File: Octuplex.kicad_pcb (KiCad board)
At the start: 2 copper layers, 140 x 140 mm, 34 parts, among them J1 DIN-5_180degree, J2 DIN-5_180degree, U1 MC68B09, U10 R6522, U11 74LS138, U12 HCPL-2631, U13 74LS251, U14 PCF8584, U15 74LS138, U2 MC68B40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

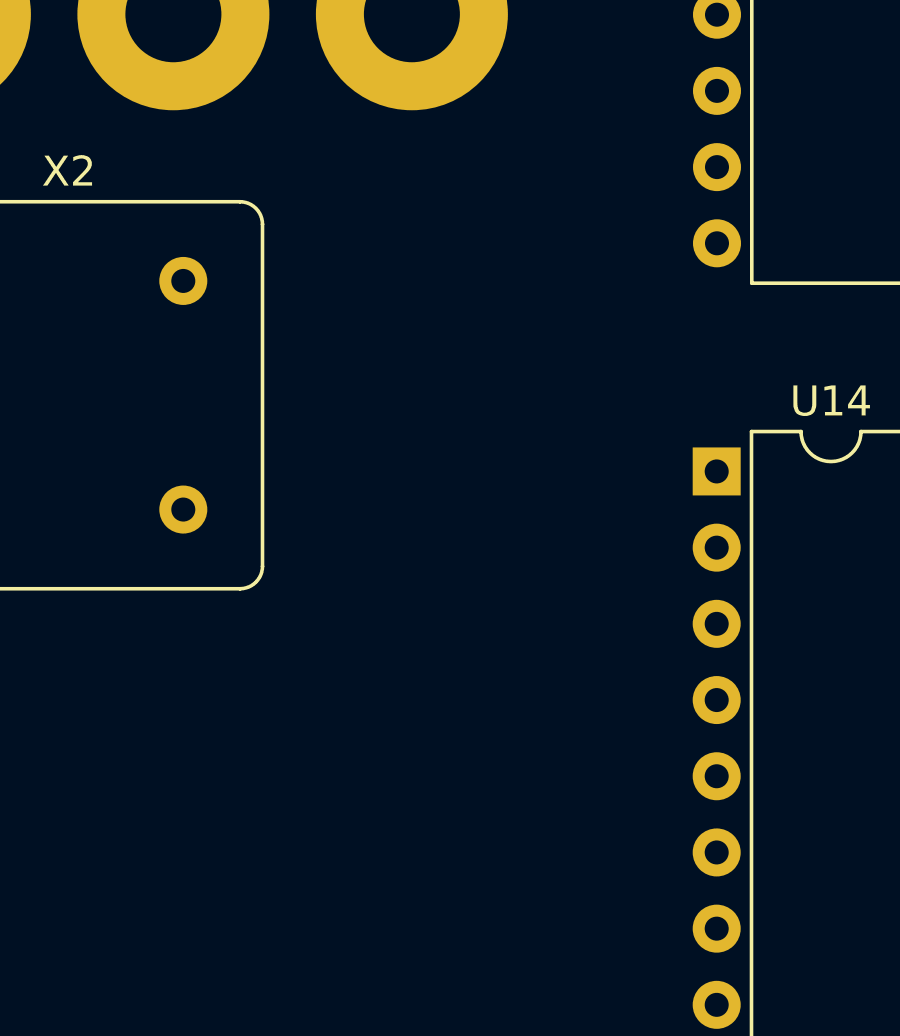
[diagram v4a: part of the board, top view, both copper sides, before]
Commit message: Add ZN428 8-bit DAC.
Add symbol for ZN428 and place it on the GPIO page.
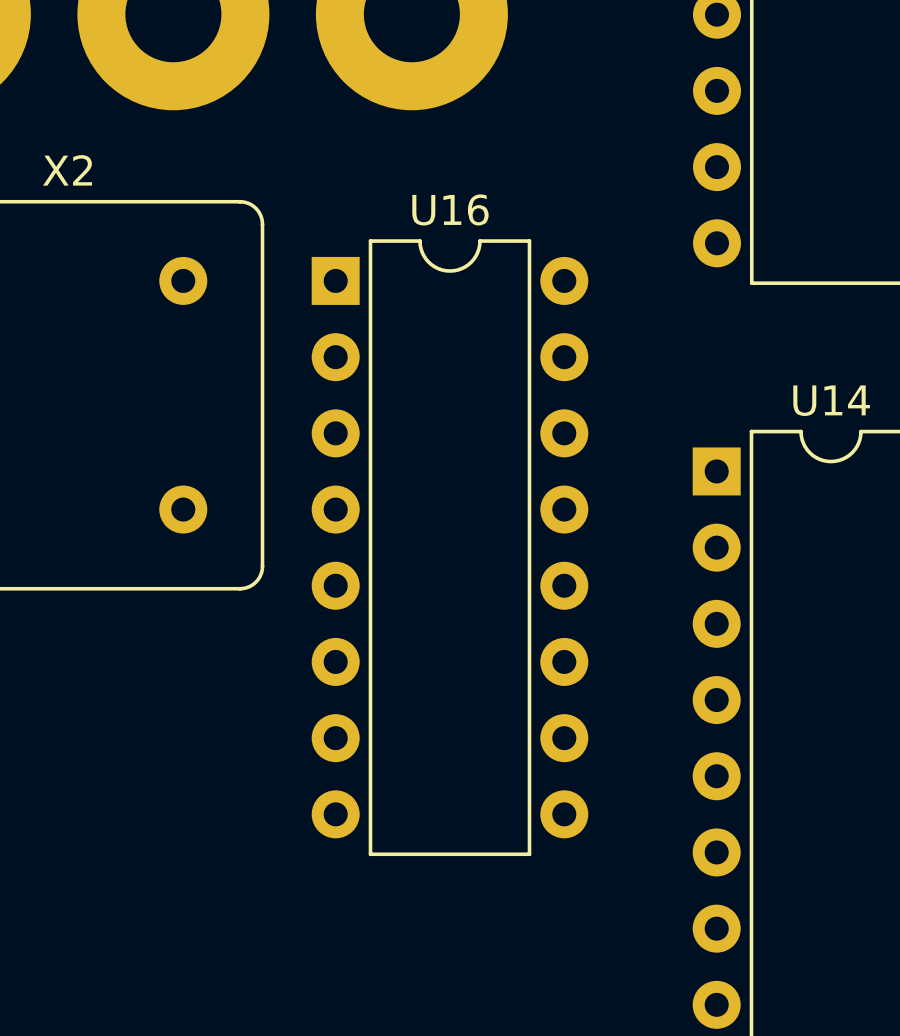
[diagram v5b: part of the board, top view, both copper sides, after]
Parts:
- added U16: ZN428, Package_DIP:DIP-16_W7.62mm, F.Cu at (255.3, 94.0)
